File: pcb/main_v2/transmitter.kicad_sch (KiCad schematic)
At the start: 24 parts, among them IC301 SE2576L-R, IC302 RMS-30+, J301 Conn_Coaxial, J302 Conn_Coaxial

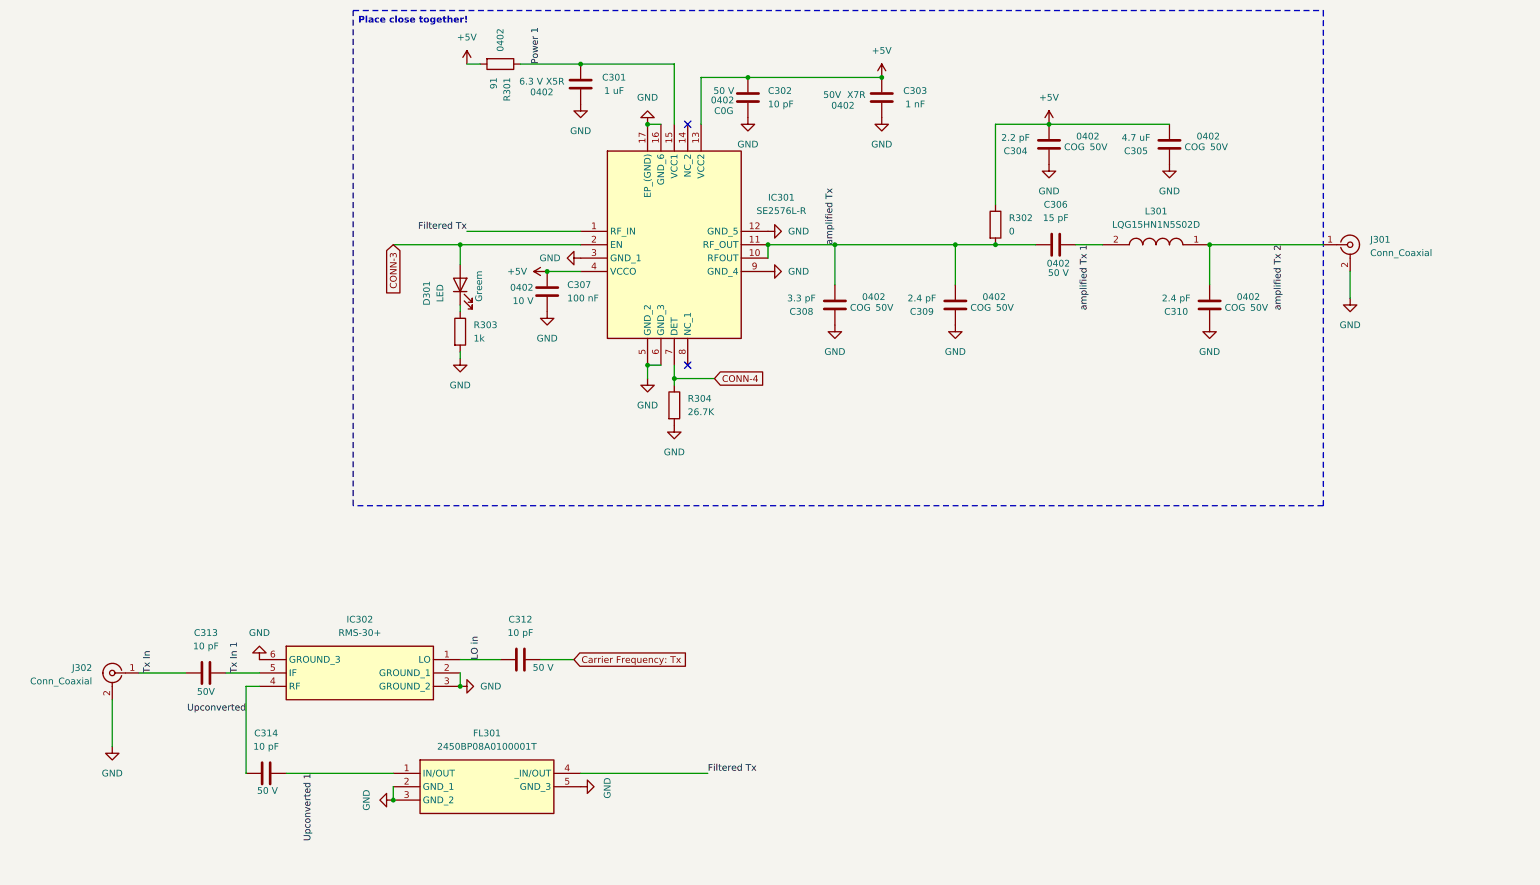
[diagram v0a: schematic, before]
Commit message: updated layout
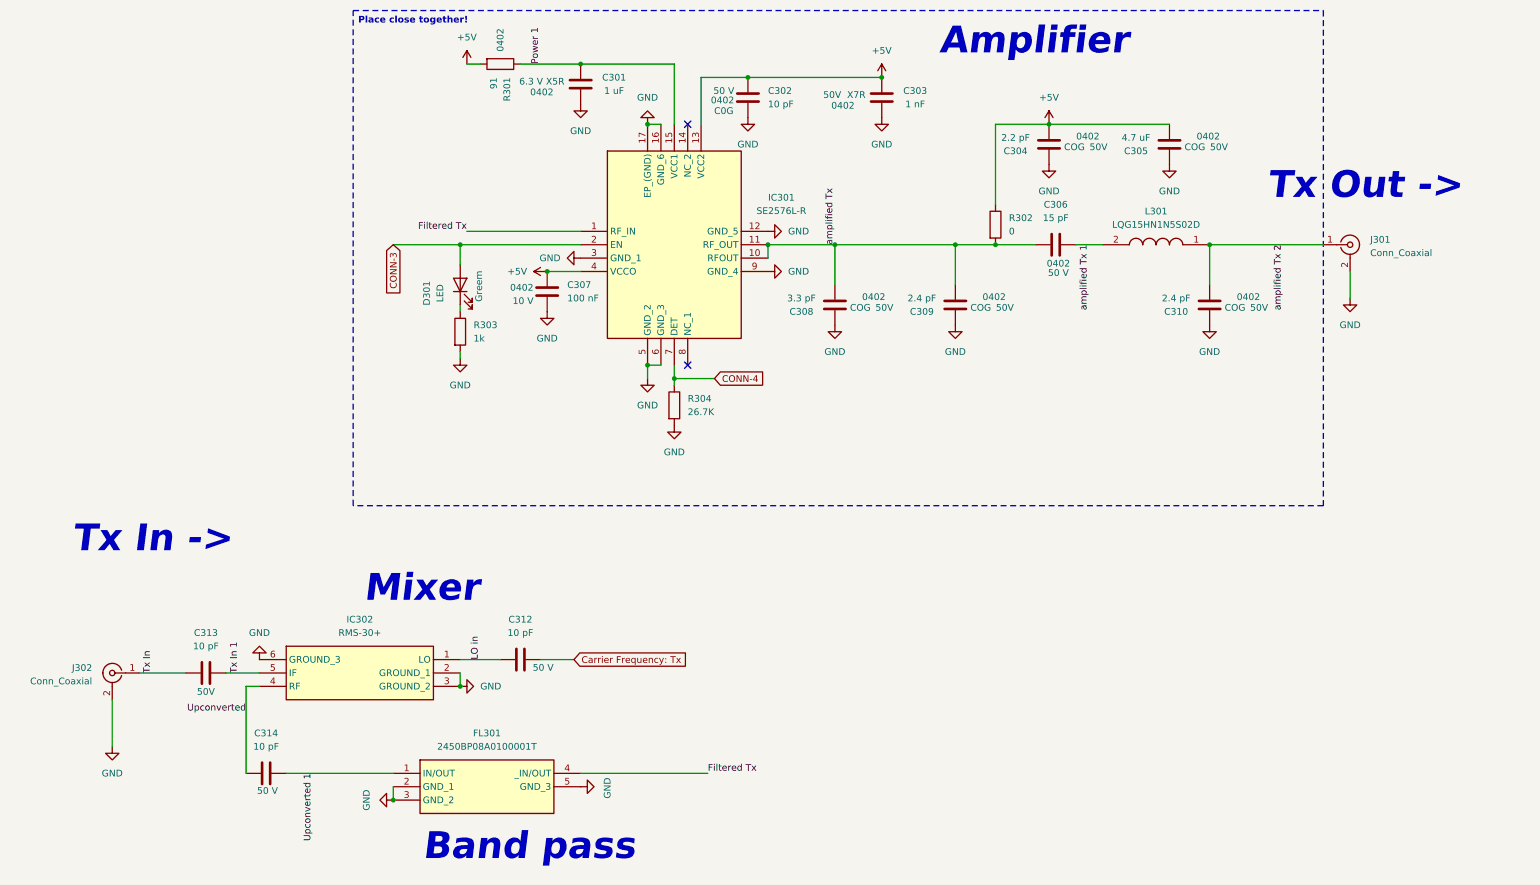
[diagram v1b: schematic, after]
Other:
- note added: "Amplifier"
- note added: "Band pass"
- note added: "Mixer"
- note added: "Tx In ->"
- note added: "Tx Out ->"
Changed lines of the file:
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@@
 	(generator_version "10.0")
 	(paper "A4")
+	(text "Tx In ->"
+		(exclude_from_sim no)
+		(at 16.51 129.54 0)
+		(effects
+			(font
+				(size 5.08 5.08)
+				(thickness 0.254)
+				(bold yes)
+				(italic yes)
+				(color 62 180 4 1)
+			)
+			(justify left)
+		)
+	)
+	(text "Amplifier"
+		(exclude_from_sim no)
+		(at 181.102 35.052 0)
+		(effects
+			(font
+				(size 5.08 5.08)
+				(thickness 0.254)
+				(bold yes)
+				(italic yes)
+				(color 62 180 4 1)
+			)
+			(justify left)
+		)
+	)
+	(text "Tx Out ->"
+		(exclude_from_sim no)
+		(at 243.332 62.484 0)
+		(effects
+			(font
+				(size 5.08 5.08)
+				(thickness 0.254)
+				(bold yes)
+				(italic yes)
+				(color 62 180 4 1)
+			)
+			(justify left)
+		)
+	)
+	(text "Mixer"
+		(exclude_from_sim no)
+		(at 71.882 138.938 0)
+		(effects
+			(font
+				(size 5.08 5.08)
+				(thickness 0.254)
+				(bold yes)
+				(italic yes)
+				(color 62 180 4 1)
+			)
+			(justify left)
+		)
+	)
+	(text "Band pass"
+		(exclude_from_sim no)
+		(at 83.058 187.96 0)
+		(effects
+			(font
+				(size 5.08 5.08)
+				(thickness 0.254)
+				(bold yes)
+				(italic yes)
+				(color 62 180 4 1)
+			)
+			(justify left)
+		)
+	)
 	(text_box "Place close together!"
 		(exclude_from_sim no)
